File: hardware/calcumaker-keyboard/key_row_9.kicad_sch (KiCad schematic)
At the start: 27 parts, among them SW31 MX, SW32 MX, SW33 MX, SW34 MX, SW35 MX, SW37 MX, SW38 MX, SW39 MX, SW40 MX

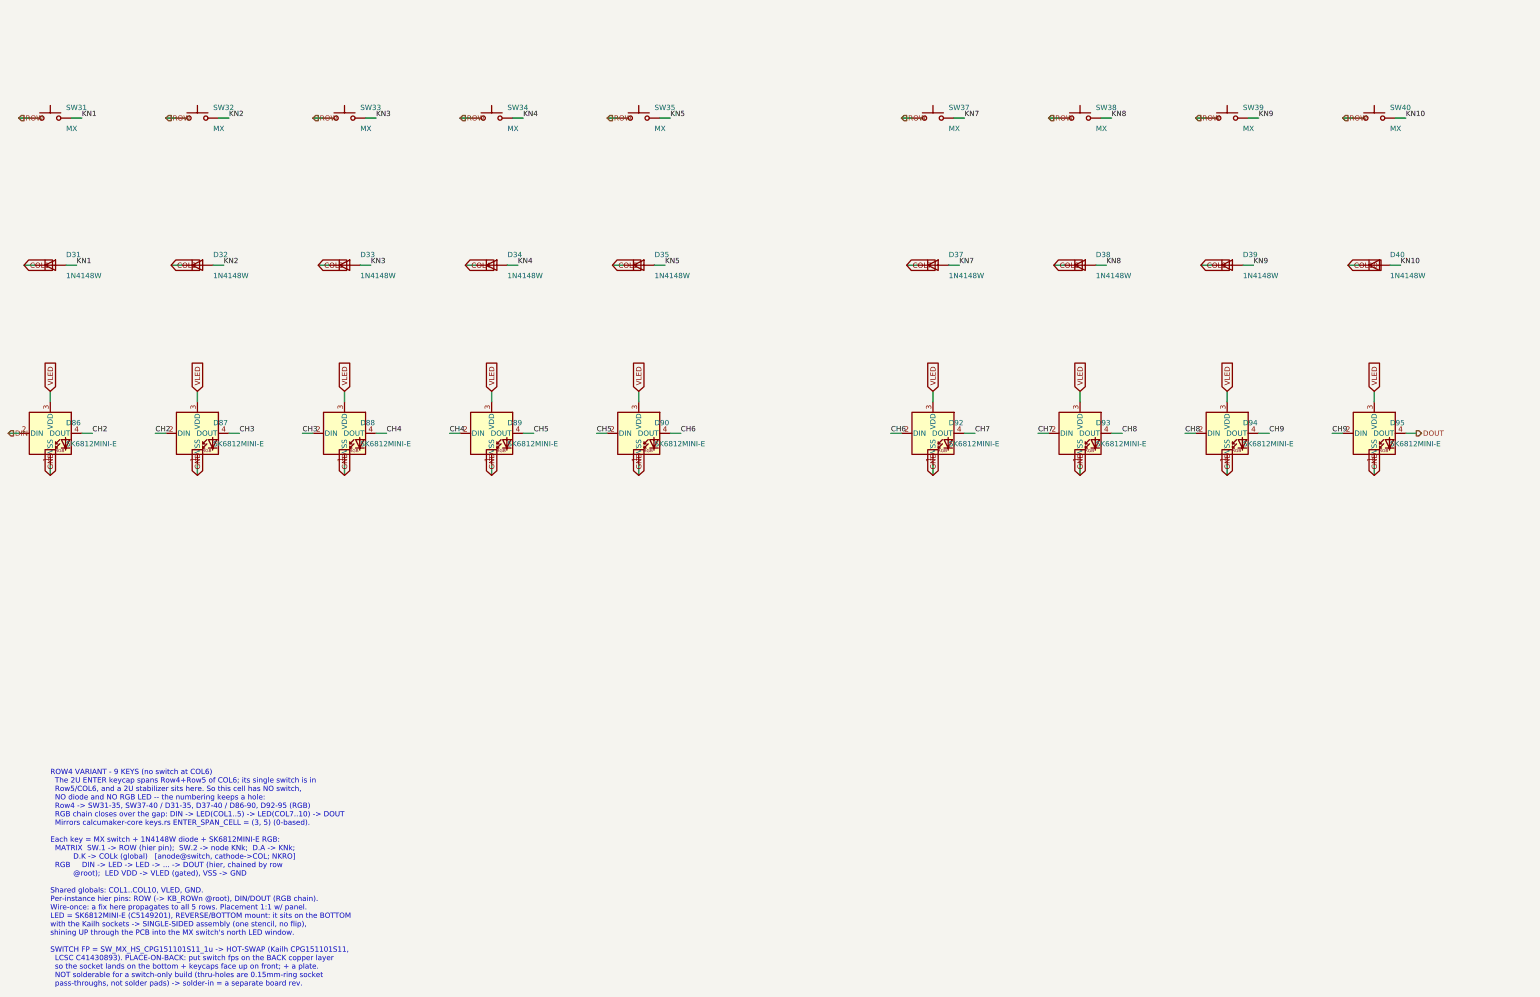
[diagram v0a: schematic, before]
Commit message: Wire mainboard and keypad schematics and verify expanded nets
Connect hierarchical interfaces, power/control circuits, debug links, matrix and RGB chains. Correct MCU package pins, diode polarity and power configuration; add bypass components and repeatable KiCad netlist/ERC checks. Document pin maps and remaining physical validation.
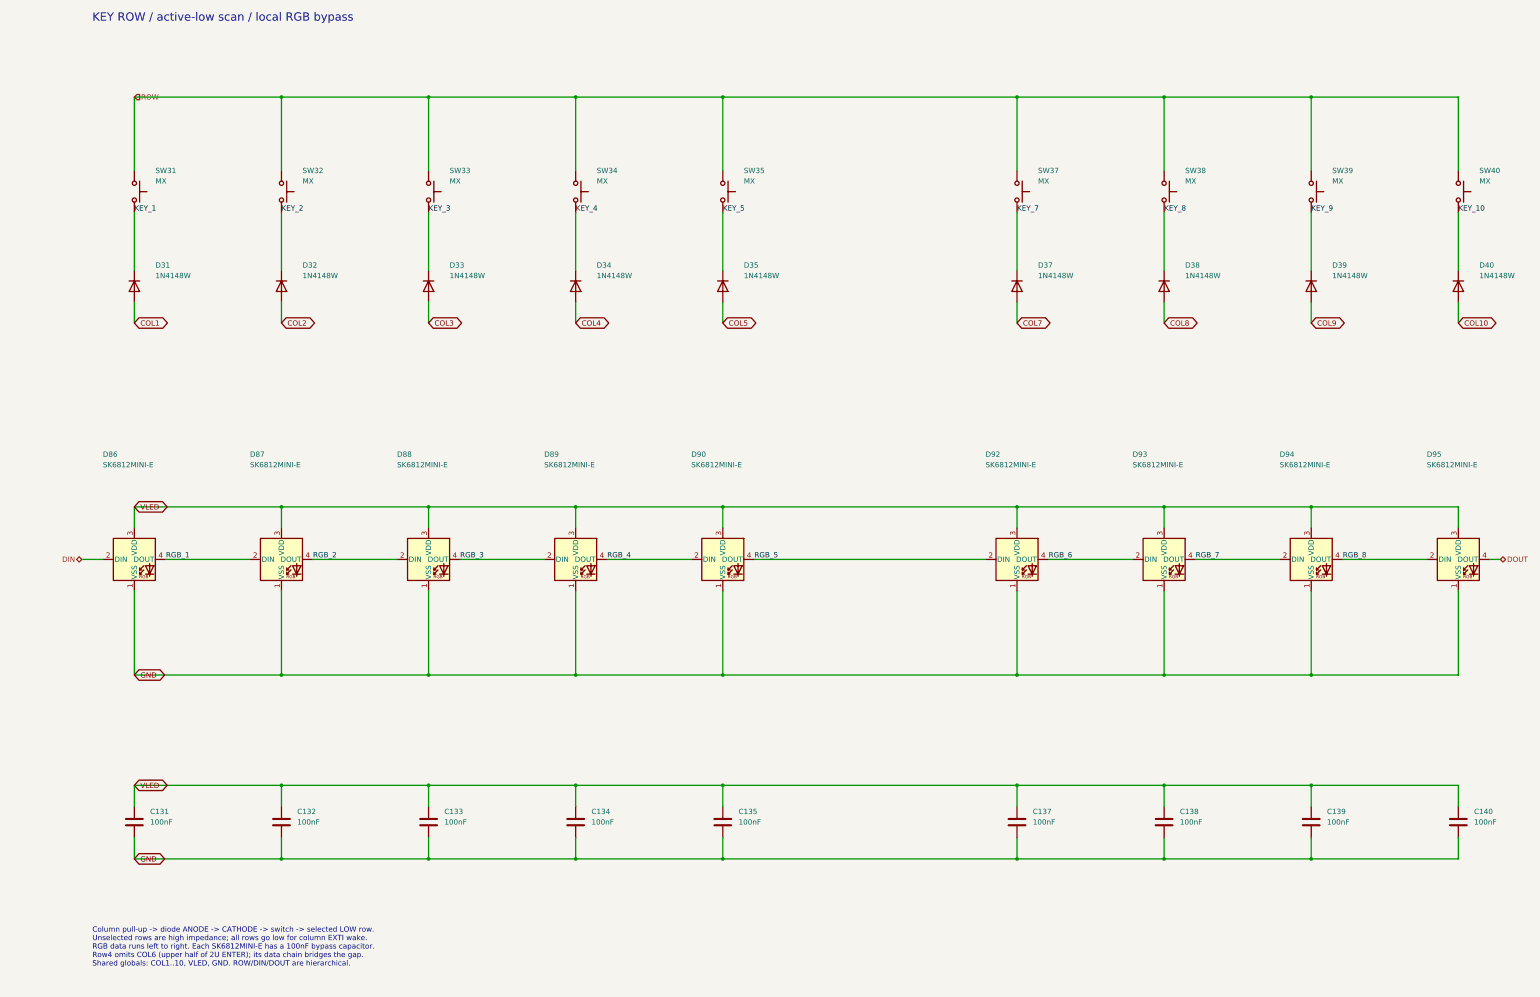
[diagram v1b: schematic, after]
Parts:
- added C131, C132, C133, C134, C135, C137, C138, C139, C140: 100nF, Capacitor_SMD:C_0402_1005Metric, symbol Device:C
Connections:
- net COL1: now also D31.2 (A); no longer D31.1 (K)
- net COL10: now also D40.2 (A); no longer D40.1 (K)
- net COL2: now also D32.2 (A); no longer D32.1 (K)
- net COL3: now also D33.2 (A); no longer D33.1 (K)
- net COL4: now also D34.2 (A); no longer D34.1 (K)
- net COL5: now also D35.2 (A); no longer D35.1 (K)
- net COL7: now also D37.2 (A); no longer D37.1 (K)
- net COL8: now also D38.2 (A); no longer D38.1 (K)
- net COL9: now also D39.2 (A); no longer D39.1 (K)
- net GND: now also C131.2, C132.2, C133.2, C134.2, C135.2, C137.2, C138.2, C139.2, C140.2
- net VLED: now also C131.1, C132.1, C133.1, C134.1, C135.1, C137.1, C138.1, C139.1, C140.1
- net CH2 renamed RGB_1
- net CH3 renamed RGB_2
- net CH4 renamed RGB_3
- net CH5 renamed RGB_4
- net CH6 renamed RGB_5
- net CH7 renamed RGB_6
- net CH8 renamed RGB_7
- net CH9 renamed RGB_8
- net KN1 renamed KEY_1
- net KEY_1: now also D31.1 (K); no longer D31.2 (A)
- net KN10 renamed KEY_10
- net KEY_10: now also D40.1 (K); no longer D40.2 (A)
- net KN2 renamed KEY_2
- net KEY_2: now also D32.1 (K); no longer D32.2 (A)
- net KN3 renamed KEY_3
- net KEY_3: now also D33.1 (K); no longer D33.2 (A)
- net KN4 renamed KEY_4
- net KEY_4: now also D34.1 (K); no longer D34.2 (A)
- net KN5 renamed KEY_5
- net KEY_5: now also D35.1 (K); no longer D35.2 (A)
- net KN7 renamed KEY_7
- net KEY_7: now also D37.1 (K); no longer D37.2 (A)
- net KN8 renamed KEY_8
- net KEY_8: now also D38.1 (K); no longer D38.2 (A)
- net KN9 renamed KEY_9
- net KEY_9: now also D39.1 (K); no longer D39.2 (A)
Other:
- note added: "Column pull-up -> diode ANODE -> CATHODE -> switch -> selected LOW row. Unselected rows are high impedance; all rows go low for column EXTI wake. RGB data runs left to right. Each SK6812MINI-E has a 100nF bypass capacitor. Row4 omits COL6 (upper half of 2U ENTER); its data chain bridges the gap. Shared globals: COL1..10, VLED, GND. ROW/DIN/DOUT are hierarchical."
- note added: "KEY ROW / active-low scan / local RGB bypass"
- note removed: "ROW4 VARIANT - 9 KEYS (no switch at COL6) The 2U ENTER keycap spans Row4+Row5 of COL6; its single switch is in Row5/COL6, and a 2U stabilizer sits here. So this cell has NO switch, NO diode and NO RGB LED -- the numbering keeps a hole: Row4 -> SW31-35, SW37-40 / D31-35, D37-40 / D86-90, D92-95 (RGB) RGB chain closes over the gap: DIN -> LED(COL1..5) -> LED(COL7..10) -> DOUT Mirrors calcumaker-cor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"
- title: Calcumaker 16 — Keyboard — Row4 variant: 9 keys (2U ENTER spans COL6 - no switch there) -> Calcumaker 16 / keyboard / key row 9
- moved on the sheet: D31, D32, D33, D34, D35, D37, D38, D39, D40, D86, D87, D88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
